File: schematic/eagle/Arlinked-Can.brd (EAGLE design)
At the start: 160 x 100 mm, 18 parts, among them U1 MCP2515, U2 TJA1050, U3 V_REG_LDOSMD, Y1 xtal

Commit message: Added schematic/protel/arlinked-can-v0.1-print-10p.pcb
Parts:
- added J8: (no value), Arlinked:JUMPER-1X3-SMD
- added R3: 10k, SparkFun:0603-RES
- added U$1: PAD, Arlinked:PAD-4MM
- C1, C3: value (none) -> 10uF
- C2: value (none) -> 407
- JP1: value (none) -> HOLE1
- JP2: value (none) -> HOLE2
- JP3: value (none) -> INPUT_HEADER
- LED1: value (none) -> 2mA
- R2: value (none) -> 320R
- moved R2 0.63 mm to (39.0, 28.3)
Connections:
- removed net N$7: F1.1, U3.5
- new net N$10: J8.J-2, R3.1
- new net S: J8.J-0, U2.8
- new net VCC-DIRECT: F1.1, JP7.J-2, U3.5
- net GND: now also J8.J-1; no longer U2.8
- net VCC: now also R3.2; no longer JP7.J-2
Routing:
- net VCC-DIRECT: track 0.00 -> 17.2 mm, vias 0 -> 3
- net N$7: track 14.1 -> 0.00 mm, vias 2 -> 0
- net S: track 0.00 -> 5.85 mm, vias 0 -> 1
- net N$10: track 0.00 -> 2.62 mm
- net N$6: track 16.1 -> 16.8 mm
- net VCC-LDO: track 17.0 -> 16.4 mm
- net SPI-SCK: track 30.6 -> 30.0 mm
- net VCC: track 39.7 -> 39.2 mm, vias 4 -> 3

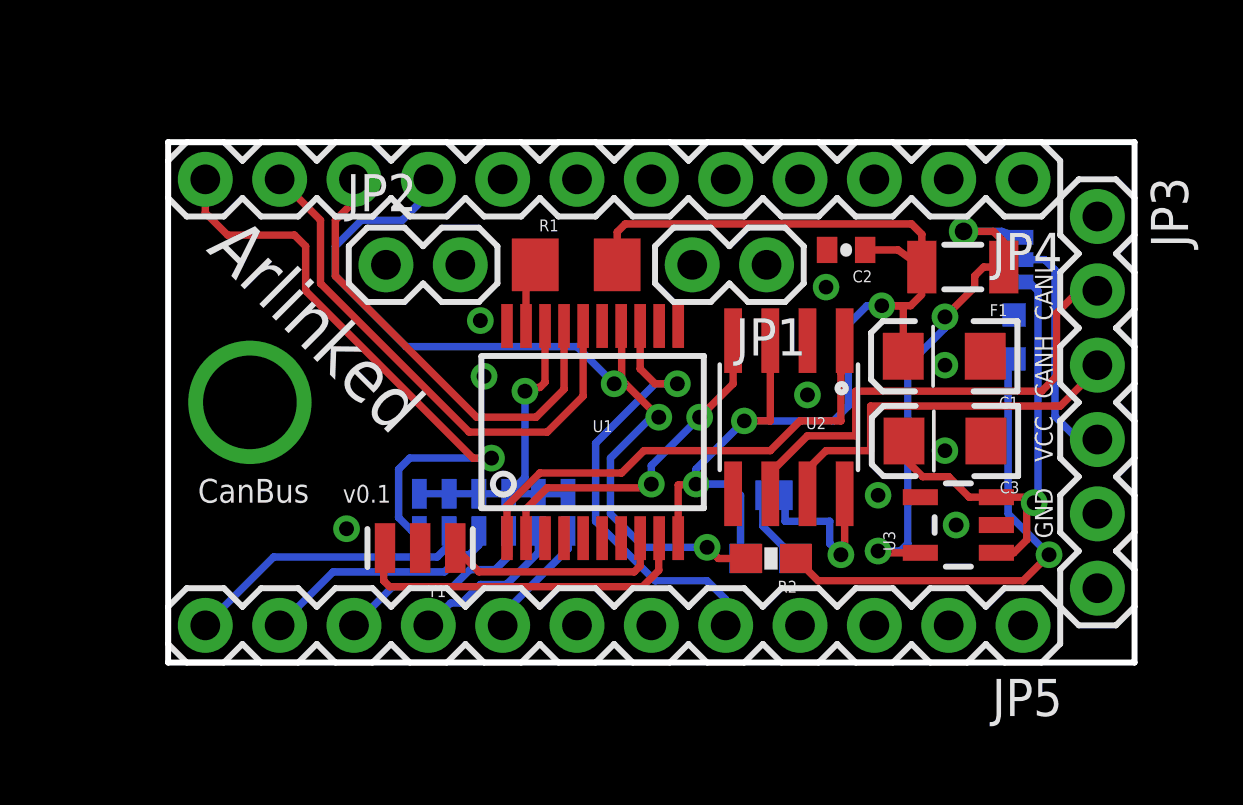
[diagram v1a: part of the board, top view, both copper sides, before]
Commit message: Added Arlinked CanBus module v0.2
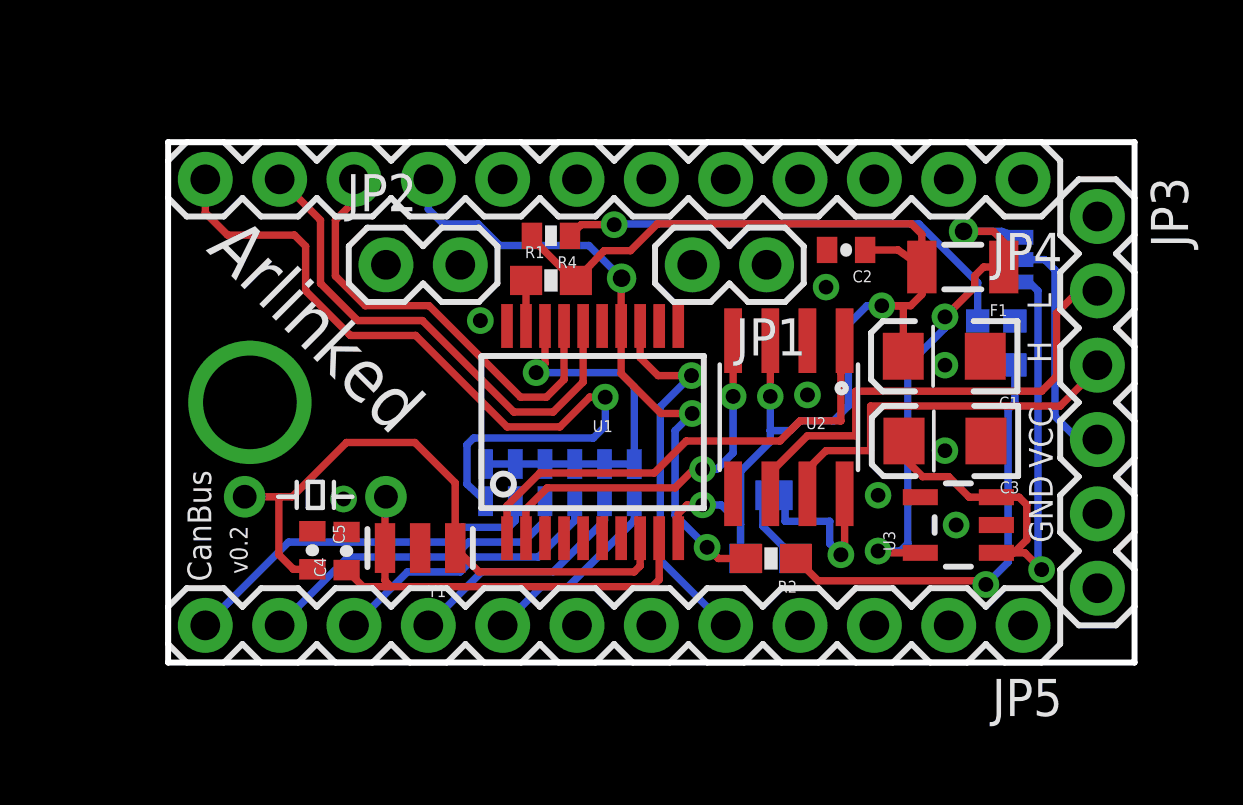
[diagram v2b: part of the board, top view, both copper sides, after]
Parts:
- added C4, C5: (no value), SparkFun:0402-CAP
- added LED2: 2mA Red, SparkFun:LED-0603
- added R4: 320R, SparkFun:0402-RES
- added Y2: (no value), Arlinked:HC49U-V
- R1: device SparkFun:1206 -> SparkFun:0603-RES
- moved U$2 2.48 mm to (31.8, 30.9)
- moved R1 1.02 mm to (31.5, 37.8)
- moved LED1 0.20 mm to (47.3, 35.7)
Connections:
- net N$6 renamed LED1-CAN-2
- net VCC-DIRECT renamed VCC-FUSE
- removed net N$3: U1.8, Y1.1
- removed net N$4: U1.9, Y1.3
- new net LED2-POWER-2: LED2.A, R4.1
- new net OSC1: C4.1, U1.9, Y1.3, Y2.2
- new net OSC2: C5.2, U1.8, Y1.1, Y2.1
- net GND: now also C4.2, C5.1, LED2.C
- net VCC: now also R4.2
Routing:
- net OSC2: track 0.00 -> 21.8 mm
- net LED2-POWER-2: track 0.00 -> 16.2 mm, vias 0 -> 1
- net OSC1: track 0.00 -> 15.6 mm
- net N$4: track 12.0 -> 0.00 mm
- net SPI-SCK: track 30.0 -> 21.6 mm
- net N$3: track 7.69 -> 0.00 mm
- net SPI-CS1: track 21.2 -> 27.3 mm
- net SPI-CS2: track 9.95 -> 14.1 mm
- net VCC-LDO: track 16.4 -> 20.0 mm
- net SPI-CS3: track 8.43 -> 11.2 mm
- net SPI-INT: track 15.7 -> 13.0 mm
- net SPI-CS5: track 5.53 -> 8.16 mm
- net SPI-CS4: track 7.13 -> 9.69 mm
- net SPI-CS6: track 4.15 -> 6.64 mm
- net VCC: track 39.2 -> 41.6 mm
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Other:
- board text added: "H"
- board text added: "L"
- board text added: "v0.2"
- board text removed: "CANH"
- board text removed: "CANL"
- board text removed: "v0.1"

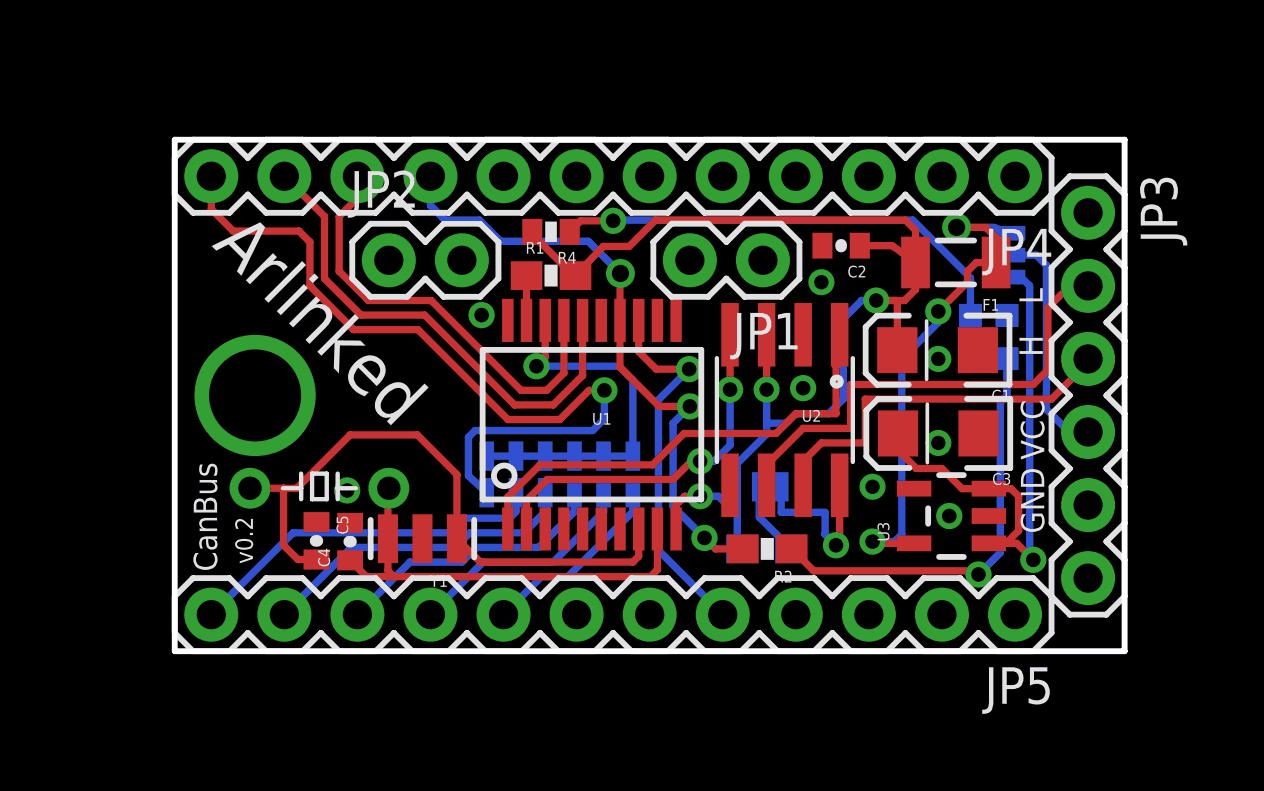
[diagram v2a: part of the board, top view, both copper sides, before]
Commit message: CanBus module v0.2 schematic and PCB release  #4 fixed Vdd Vss mistake
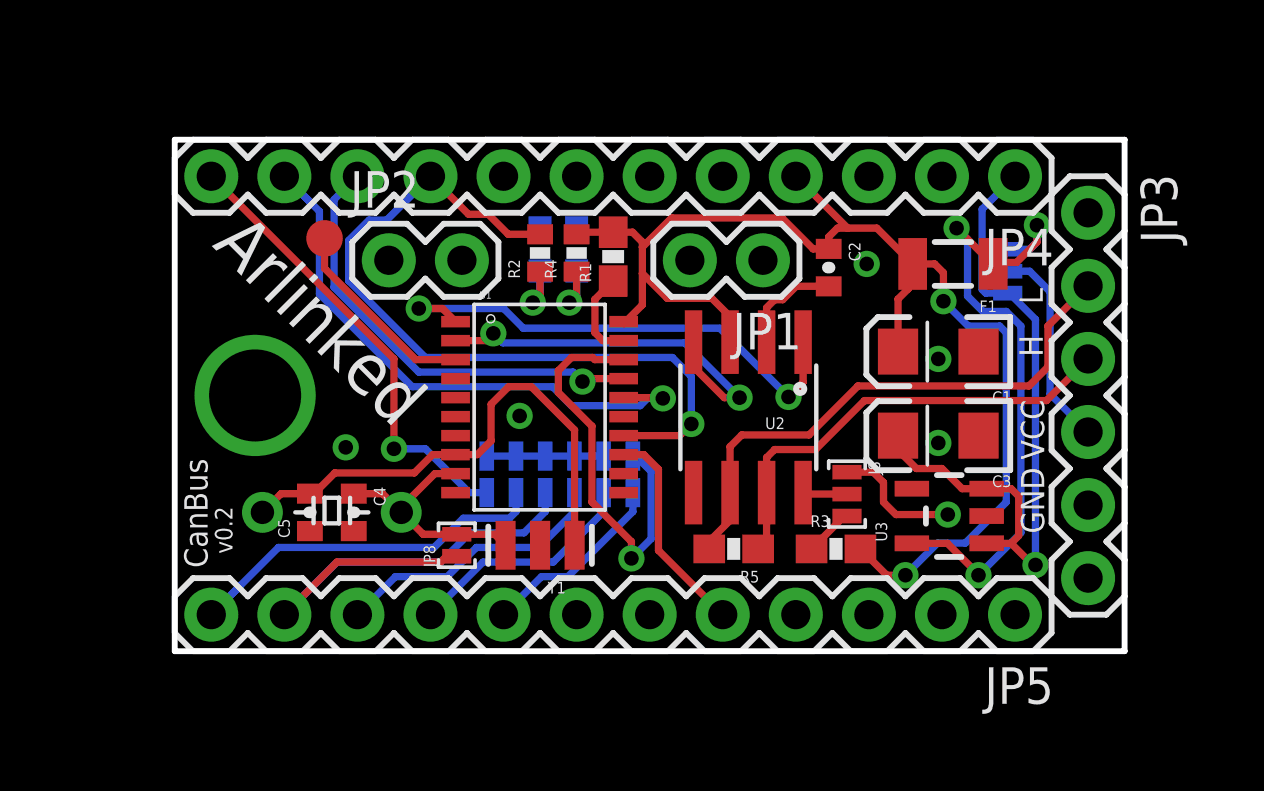
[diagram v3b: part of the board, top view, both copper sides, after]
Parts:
- added JP8: JUMPER-1X2, Arlinked:JUMPER-1X2-SMD-10
- added R5: (no value), SparkFun:0603-RES
- added U$3: PAD_SMD, Arlinked:PAD-SMD-2MM
- C2: value 407 -> 0.1uF
- J8: value (none) -> JUMPER-1X3; device Arlinked:JUMPER-1X3-SMD -> Arlinked:JUMPER-1X3-SMD-10
- JP7: device Arlinked:JUMPER-1X3-SMD -> Arlinked:JUMPER-1X3-SMD-10
- LED1: value 2mA -> Green
- LED2: value 2mA Red -> Red
- R2: value 320R -> 2~10K; device SparkFun:0603-RES -> SparkFun:0402-RES
- R4: value 320R -> 2~10K
- U$1: device Arlinked:PAD-4MM -> Arlinked:PAD-HOLE-4MM
- U1: value MCP2515 -> MCP2515-20P; device Arlinked:SSOP-20 -> Arlinked:TSSOP20
- moved LED1 16.5 mm to (31.1, 38.7)
- moved LED2 14.0 mm to (32.4, 38.7), turned to 0 degrees
- moved R2 13.0 mm to (31.1, 38.6), turned to 90 degrees
- moved Y1 4.10 mm to (31.1, 28.4)
- moved R3 2.41 mm to (41.4, 28.3), flipped to the top
- moved J8 2.30 mm to (41.8, 30.2), flipped to the top, turned to 270 degrees
- moved R1 2.26 mm to (33.7, 38.5), turned to 90 degrees
- moved U1 2.01 mm to (31.1, 33.5)
- moved U2 1.30 mm to (38.4, 32.9)
- moved R4 1.15 mm to (32.4, 38.6), turned to 90 degrees
- moved C4 1.02 mm to (24.6, 29.6), turned to 270 degrees
- moved C5 1.02 mm to (23.1, 29.6), turned to 90 degrees
- moved Y2 0.94 mm to (23.9, 29.6)
- moved C2 0.88 mm to (41.1, 38.1), turned to 270 degrees
- moved JP7 0.57 mm to (47.4, 38.0)
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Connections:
- new net CLKOUT: U$3.P$1, U1.3
- net CANH: now also R5.1
- net CANL: now also R5.2
- net GND: now also JP4.2, JP5.4, U1.10; no longer U1.20
- net OSC1: now also JP8.J-0
- net SPI-CS3: now also JP8.J-1
- net VCC: now also JP4.4, U1.20; no longer U1.10
- net VCC-LDO: now also JP4.1
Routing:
- net LED2-POWER-2: track 16.2 -> 2.39 mm
- net LED1-CAN-2: track 14.8 -> 2.39 mm
- net SPI-CS1: track 27.3 -> 16.0 mm
- net GND: track 0.00 -> 8.18 mm, vias 8 -> 6
- net OSC1: track 15.6 -> 8.57 mm
- net CLKOUT: track 0.00 -> 6.91 mm
- net SPI-CS3: track 11.2 -> 18.0 mm
- net SPI-CS: track 13.0 -> 19.3 mm
- net SPI-SCK: track 21.6 -> 27.3 mm, vias 3 -> 1
- net VCC-FUSE: track 17.2 -> 22.8 mm
- net SPI-INT: track 13.0 -> 7.39 mm, vias 1 -> 0
- net VCC-LDO: track 20.0 -> 24.3 mm
- net S: track 5.85 -> 1.55 mm, vias 1 -> 0
- net OSC2: track 21.8 -> 18.0 mm
- net SPI-SI: track 17.3 -> 20.9 mm, vias 0 -> 1
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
